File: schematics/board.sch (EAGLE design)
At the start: 25 parts, among them IC1 MEGA8-P, M1 PSMN017-30ELL-V, M2 PSMN017-30ELL-V, M3 PSMN017-30ELL-V

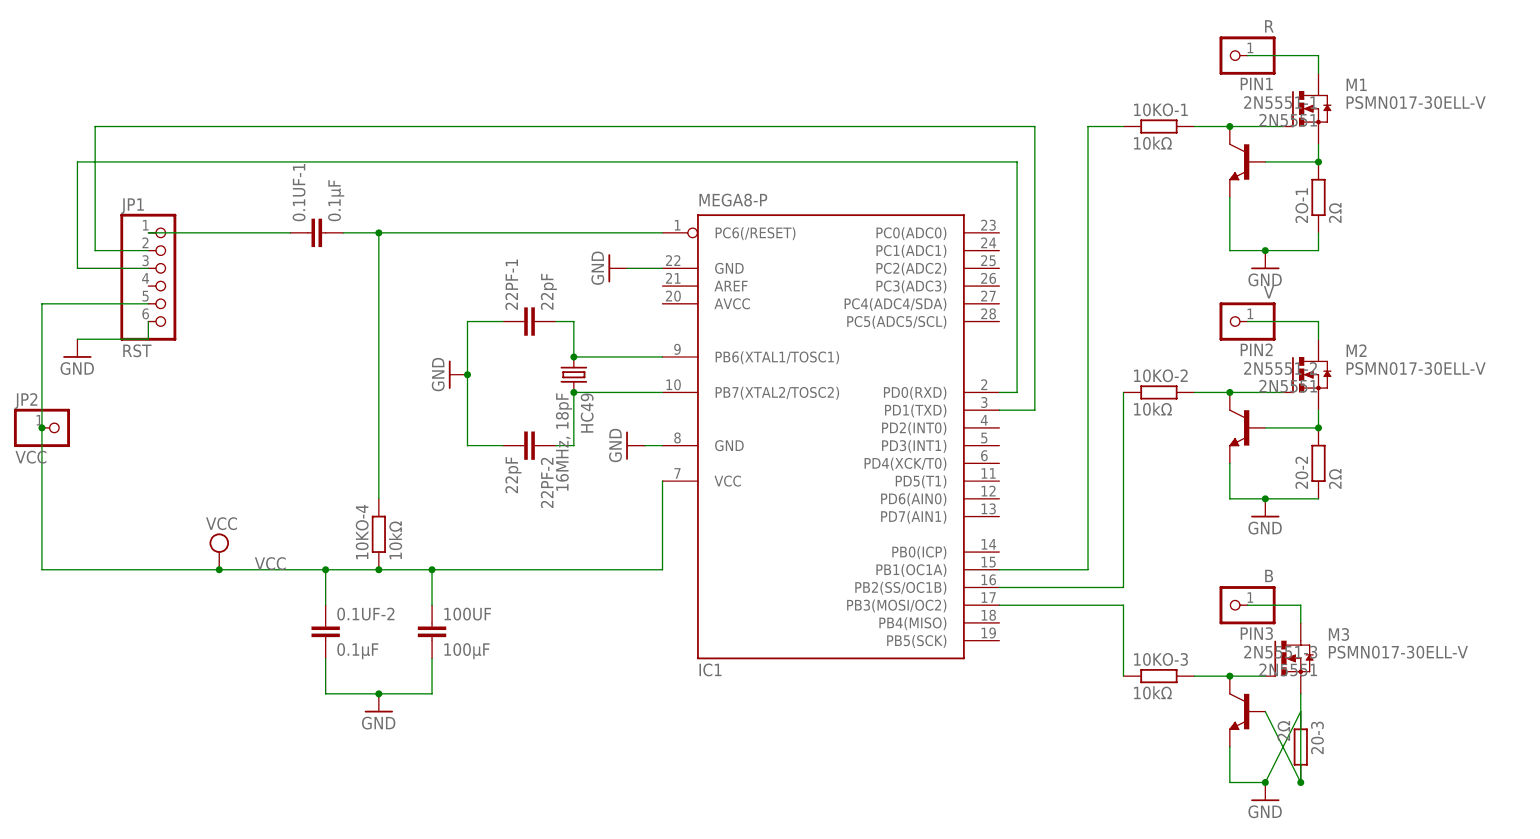
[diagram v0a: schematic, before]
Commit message: Ajoute alim & logo sur la PCB
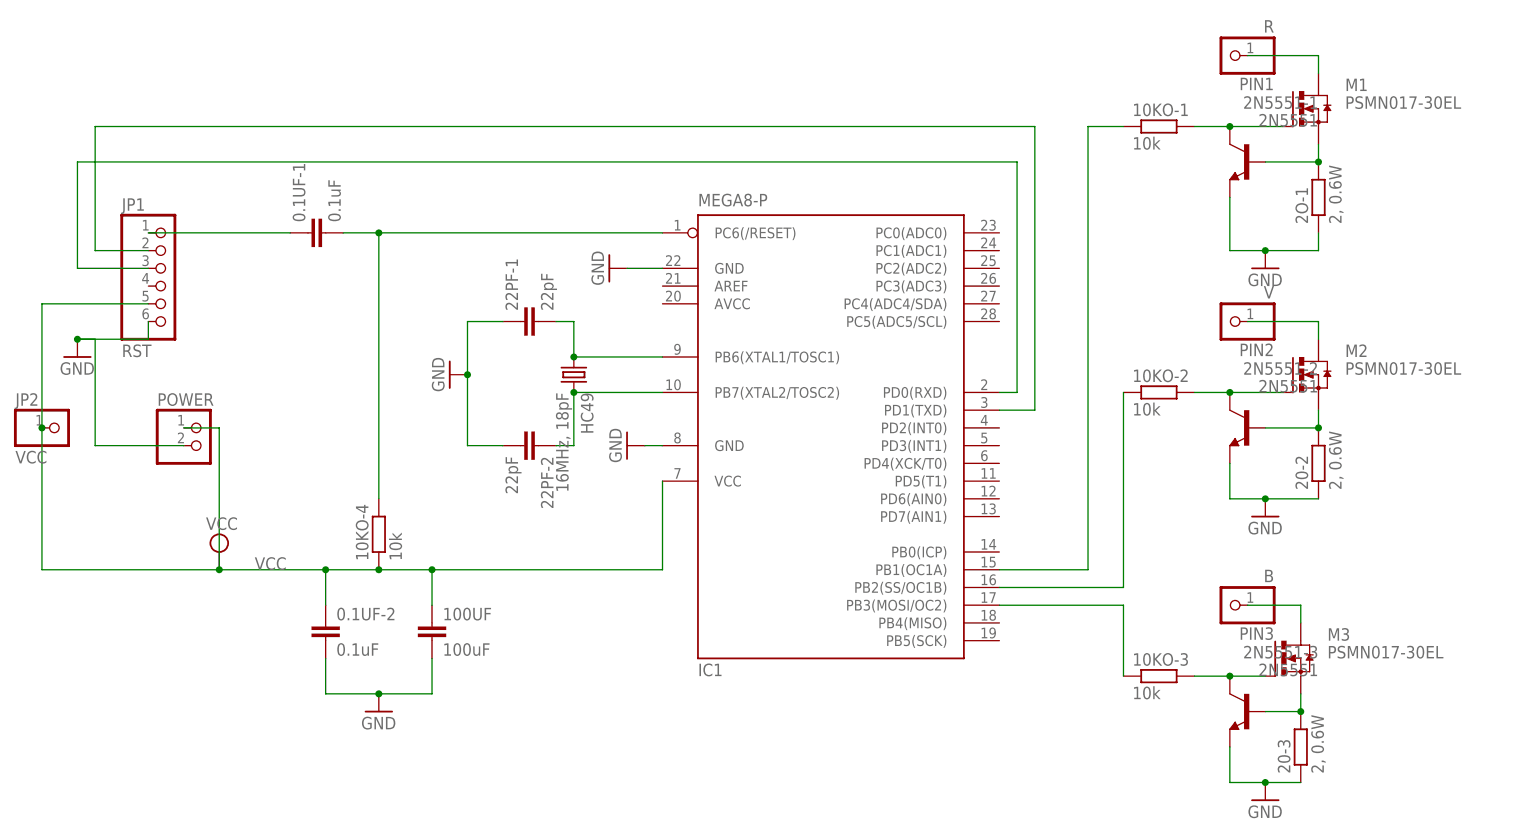
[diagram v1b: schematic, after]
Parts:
- added POWER: (no value), pinhead:PINHD-1X2
- 0.1UF-1, 0.1UF-2: value 0.1μF -> 0.1uF
- 100UF: value 100μF -> 100uF
- 10KO-1, 10KO-2, 10KO-3, 10KO-4: value 10kΩ -> 10k
- 20-2, 20-3, 2O-1: value 2Ω -> 2, 0.6W
- M1, M2, M3: value PSMN017-30ELL-V -> PSMN017-30EL
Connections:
- net GND: now also POWER.2
- net VCC: now also POWER.1
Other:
- moved on the sheet: 20-3
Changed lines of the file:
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@@
 <parts>
 <part name="IC1" library="atmel" deviceset="MEGA8-P" device=""/>
-<part name="10KO-1" library="rcl" deviceset="R-EU_" device="0207/2V" value="10kΩ"/>
-<part name="10KO-2" library="rcl" deviceset="R-EU_" device="0207/2V" value="10kΩ"/>
-<part name="10KO-3" library="rcl" deviceset="R-EU_" device="0207/2V" value="10kΩ"/>
-<part name="10KO-4" library="rcl" deviceset="R-EU_" device="0207/2V" value="10kΩ"/>
-<part name="2O-1" library="rcl" deviceset="R-EU_" device="0309/V" value="2Ω"/>
-<part name="20-2" library="rcl" deviceset="R-EU_" device="0309/V" value="2Ω"/>
-<part name="20-3" library="rcl" deviceset="R-EU_" device="0309/V" value="2Ω"/>
+<part name="10KO-1" library="rcl" deviceset="R-EU_" device="0207/2V" value="10k"/>
+<part name="10KO-2" library="rcl" deviceset="R-EU_" device="0207/2V" value="10k"/>
+<part name="10KO-3" library="rcl" deviceset="R-EU_" device="0207/2V" value="10k"/>
+<part name="10KO-4" library="rcl" deviceset="R-EU_" device="0207/2V" value="10k"/>
+<part name="2O-1" library="rcl" deviceset="R-EU_" device="0309/V" value="2, 0.6W"/>
+<part name="20-2" library="rcl" deviceset="R-EU_" device="0309/V" value="2, 0.6W"/>
+<part name="20-3" library="rcl" deviceset="R-EU_" device="0309/V" value="2, 0.6W"/>
 <part name="2N5551-1" library="transistor" deviceset="*-NPN-" device="TO92-CBE" technology="2N5551" value="2N5551"/>
 <part name="2N5551-2" library="transistor" deviceset="*-NPN-" device="TO92-CBE" technology="2N5551" value="2N5551"/>
 <part name="2N5551-3" library="transistor" deviceset="*-NPN-" device="TO92-CBE" technology="2N5551" value="2N5551"/>
-<part name="0.1UF-1" library="rcl" deviceset="C-EU" device="025-030X050" value="0.1μF"/>
-<part name="0.1UF-2" library="rcl" deviceset="C-EU" device="025-030X050" value="0.1μF"/>
+<part name="0.1UF-1" library="rcl" deviceset="C-EU" device="025-030X050" value="0.1uF"/>
+<part name="0.1UF-2" library="rcl" deviceset="C-EU" device="025-030X050" value="0.1uF"/>
 <part name="22PF-2" library="rcl" deviceset="C-EU" device="025-030X050" value="22pF"/>
 <part name="22PF-1" library="rcl" deviceset="C-EU" device="025-030X050" value="22pF"/>
-<part name="100UF" library="rcl" deviceset="C-EU" device="025-050X050" value="100μF"/>
+<part name="100UF" library="rcl" deviceset="C-EU" device="025-050X050" value="100uF"/>
 <part name="HC49" library="crystal" deviceset="CRYSTAL" device="HC49S" value="16MHz, 18pF"/>
 <part name="GND1" library="supply1" deviceset="GND" device=""/>
@@
 <part name="PIN2" library="pinhead" deviceset="PINHD-1X1" device="" value="V"/>
 <part name="PIN3" library="pinhead" deviceset="PINHD-1X1" device="" value="B"/>
-<part name="M1" library="hackens" deviceset="PSMN017-30EL" device="L-V"/>
-<part name="M2" library="hackens" deviceset="PSMN017-30EL" device="L-V"/>
-<part name="M3" library="hackens" deviceset="PSMN017-30EL" device="L-V"/>
+<part name="M1" library="hackens" deviceset="PSMN017-30EL" device="L-V" value="PSMN017-30EL"/>
+<part name="M2" library="hackens" deviceset="PSMN017-30EL" device="L-V" value="PSMN017-30EL"/>
+<part name="M3" library="hackens" deviceset="PSMN017-30EL" device="L-V" value="PSMN017-30EL"/>
+<part name="POWER" library="pinhead" deviceset="PINHD-1X2" device=""/>
 </parts>
 <sheets>
@@
 <instance part="2O-1" gate="G$1" x="149.86" y="93.98" rot="R90"/>
 <instance part="20-2" gate="G$1" x="149.86" y="55.88" rot="R90"/>
-<instance part="20-3" gate="G$1" x="147.32" y="15.24" rot="R270"/>
+<instance part="20-3" gate="G$1" x="147.32" y="15.24" rot="R90"/>
 <instance part="2N5551-1" gate="G$1" x="139.7" y="99.06" rot="MR0"/>
 <instance part="2N5551-2" gate="G$1" x="139.7" y="60.96" rot="MR0"/>
@@
 <instance part="M2" gate="G$1" x="147.32" y="68.58"/>
 <instance part="M3" gate="G$1" x="144.78" y="27.94"/>
+<instance part="POWER" gate="G$1" x="-10.16" y="58.42"/>
 </instances>
 <busses>
@@
 <wire x1="137.16" y1="10.16" x2="142.24" y2="10.16" width="0.1524" layer="91"/>
 <pinref part="20-3" gate="G$1" pin="1"/>
-<wire x1="142.24" y1="10.16" x2="147.32" y2="20.32" width="0.1524" layer="91"/>
+<wire x1="142.24" y1="10.16" x2="147.32" y2="10.16" width="0.1524" layer="91"/>
 <junction x="142.24" y="10.16"/>
 </segment>
@@
 <wire x1="-27.94" y1="73.66" x2="-17.78" y2="73.66" width="0.1524" layer="91"/>
 <wire x1="-17.78" y1="73.66" x2="-17.78" y2="76.2" width="0.1524" layer="91"/>
+<wire x1="-27.94" y1="73.66" x2="-25.4" y2="73.66" width="0.1524" layer="91"/>
+<wire x1="-25.4" y1="73.66" x2="-25.4" y2="58.42" width="0.1524" layer="91"/>
+<junction x="-27.94" y="73.66"/>
+<pinref part="POWER" gate="G$1" pin="2"/>
+<wire x1="-25.4" y1="58.42" x2="-12.7" y2="58.42" width="0.1524" layer="91"/>
 </segment>
 <segment>
@@
 <pinref part="2N5551-3" gate="G$1" pin="B"/>
 <pinref part="20-3" gate="G$1" pin="2"/>
-<wire x1="142.24" y1="20.32" x2="147.32" y2="10.16" width="0.1524" layer="91"/>
-<wire x1="147.32" y1="10.16" x2="147.32" y2="22.86" width="0.1524" layer="91"/>
-<junction x="147.32" y="10.16"/>
+<wire x1="142.24" y1="20.32" x2="147.32" y2="20.32" width="0.1524" layer="91"/>
+<wire x1="147.32" y1="20.32" x2="147.32" y2="22.86" width="0.1524" layer="91"/>
+<junction x="147.32" y="20.32"/>
 <pinref part="M3" gate="G$1" pin="S"/>
 </segment>
@@
 <junction x="-33.02" y="60.96"/>
 <junction x="-7.62" y="40.64"/>
-</segment>
-</net>
+<wire x1="-7.62" y1="40.64" x2="-7.62" y2="60.96" width="0.1524" layer="91"/>
+<pinref part="POWER" gate="G$1" pin="1"/>
+<wire x1="-7.62" y1="60.96" x2="-12.7" y2="60.96" width="0.1524" layer="91"/>
+</segment>
+</net>

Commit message: Ajout pins upload
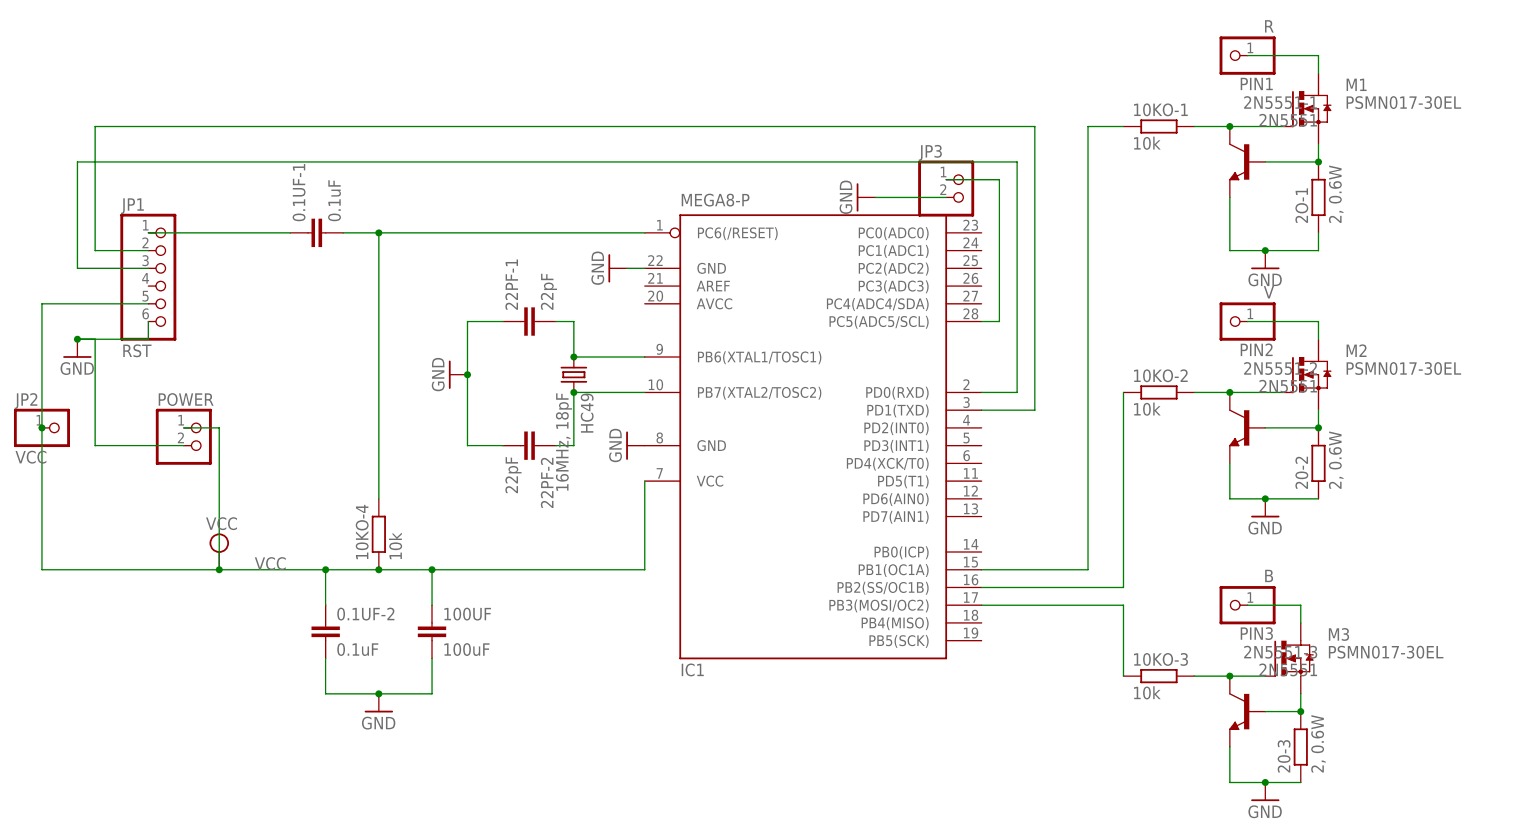
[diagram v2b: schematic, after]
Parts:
- added JP3: (no value), pinhead:PINHD-1X2
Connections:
- new net N$19: IC1.PC5(ADC5/SCL), JP3.1
- net GND: now also JP3.2
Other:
- moved on the sheet: IC1
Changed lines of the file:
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@@
 <part name="M3" library="hackens" deviceset="PSMN017-30EL" device="L-V" value="PSMN017-30EL"/>
 <part name="POWER" library="pinhead" deviceset="PINHD-1X2" device=""/>
+<part name="JP3" library="pinhead" deviceset="PINHD-1X2" device=""/>
+<part name="GND9" library="supply1" deviceset="GND" device=""/>
 </parts>
 <sheets>
@@
 </plain>
 <instances>
-<instance part="IC1" gate="G$1" x="78.74" y="60.96"/>
+<instance part="IC1" gate="G$1" x="76.2" y="60.96"/>
 <instance part="10KO-1" gate="G$1" x="127" y="104.14"/>
 <instance part="10KO-2" gate="G$1" x="127" y="66.04"/>
@@
 <instance part="M3" gate="G$1" x="144.78" y="27.94"/>
 <instance part="POWER" gate="G$1" x="-10.16" y="58.42"/>
+<instance part="JP3" gate="G$1" x="99.06" y="93.98"/>
+<instance part="GND9" gate="1" x="83.82" y="93.98" rot="R270"/>
 </instances>
 <busses>
@@
 <pinref part="GND4" gate="1" pin="GND"/>
 <pinref part="IC1" gate="G$1" pin="GND"/>
-<wire x1="50.8" y1="83.82" x2="55.88" y2="83.82" width="0.1524" layer="91"/>
+<wire x1="50.8" y1="83.82" x2="53.34" y2="83.82" width="0.1524" layer="91"/>
 </segment>
 <segment>
 <pinref part="IC1" gate="G$1" pin="GND@1"/>
 <pinref part="GND5" gate="1" pin="GND"/>
-<wire x1="55.88" y1="58.42" x2="53.34" y2="58.42" width="0.1524" layer="91"/>
 </segment>
 <segment>
@@
 <wire x1="27.94" y1="76.2" x2="33.02" y2="76.2" width="0.1524" layer="91"/>
 </segment>
+<segment>
+<pinref part="JP3" gate="G$1" pin="2"/>
+<wire x1="96.52" y1="93.98" x2="86.36" y2="93.98" width="0.1524" layer="91"/>
+<pinref part="GND9" gate="1" pin="GND"/>
+</segment>
 </net>
 <net name="N$5" class="0">
@@
 <wire x1="10.16" y1="88.9" x2="15.24" y2="88.9" width="0.1524" layer="91"/>
 <pinref part="10KO-4" gate="G$1" pin="2"/>
-<wire x1="15.24" y1="88.9" x2="55.88" y2="88.9" width="0.1524" layer="91"/>
+<wire x1="15.24" y1="88.9" x2="53.34" y2="88.9" width="0.1524" layer="91"/>
 <wire x1="15.24" y1="50.8" x2="15.24" y2="88.9" width="0.1524" layer="91"/>
 <junction x="15.24" y="88.9"/>
@@
 <segment>
 <pinref part="IC1" gate="G$1" pin="PB1(OC1A)"/>
-<wire x1="104.14" y1="40.64" x2="116.84" y2="40.64" width="0.1524" layer="91"/>
+<wire x1="101.6" y1="40.64" x2="116.84" y2="40.64" width="0.1524" layer="91"/>
 <wire x1="116.84" y1="40.64" x2="116.84" y2="104.14" width="0.1524" layer="91"/>
 <pinref part="10KO-1" gate="G$1" pin="1"/>
@@
 <pinref part="IC1" gate="G$1" pin="PB2(SS/OC1B)"/>
 <pinref part="10KO-2" gate="G$1" pin="1"/>
-<wire x1="104.14" y1="38.1" x2="121.92" y2="38.1" width="0.1524" layer="91"/>
+<wire x1="101.6" y1="38.1" x2="121.92" y2="38.1" width="0.1524" layer="91"/>
 <wire x1="121.92" y1="38.1" x2="121.92" y2="66.04" width="0.1524" layer="91"/>
 </segment>
@@
 <pinref part="IC1" gate="G$1" pin="PB3(MOSI/OC2)"/>
 <pinref part="10KO-3" gate="G$1" pin="1"/>
-<wire x1="104.14" y1="35.56" x2="121.92" y2="35.56" width="0.1524" layer="91"/>
+<wire x1="101.6" y1="35.56" x2="121.92" y2="35.56" width="0.1524" layer="91"/>
 <wire x1="121.92" y1="35.56" x2="121.92" y2="25.4" width="0.1524" layer="91"/>
 </segment>
@@
 <wire x1="22.86" y1="40.64" x2="22.86" y2="35.56" width="0.1524" layer="91"/>
 <pinref part="IC1" gate="G$1" pin="VCC@1"/>
-<wire x1="22.86" y1="40.64" x2="55.88" y2="40.64" width="0.1524" layer="91"/>
-<wire x1="55.88" y1="40.64" x2="55.88" y2="53.34" width="0.1524" layer="91"/>
+<wire x1="22.86" y1="40.64" x2="53.34" y2="40.64" width="0.1524" layer="91"/>
+<wire x1="53.34" y1="40.64" x2="53.34" y2="53.34" width="0.1524" layer="91"/>
 <junction x="22.86" y="40.64"/>
 <pinref part="SUPPLY2" gate="G$1" pin="VCC"/>
@@
 <wire x1="109.22" y1="104.14" x2="109.22" y2="63.5" width="0.1524" layer="91"/>
 <pinref part="IC1" gate="G$1" pin="PD1(TXD)"/>
-<wire x1="109.22" y1="63.5" x2="104.14" y2="63.5" width="0.1524" layer="91"/>
+<wire x1="109.22" y1="63.5" x2="101.6" y2="63.5" width="0.1524" layer="91"/>
 </segment>
 </net>
@@
 <segment>
 <pinref part="IC1" gate="G$1" pin="PD0(RXD)"/>
-<wire x1="104.14" y1="66.04" x2="106.68" y2="66.04" width="0.1524" layer="91"/>
+<wire x1="101.6" y1="66.04" x2="106.68" y2="66.04" width="0.1524" layer="91"/>
 <wire x1="106.68" y1="66.04" x2="106.68" y2="99.06" width="0.1524" layer="91"/>
 <wire x1="106.68" y1="99.06" x2="-27.94" y2="99.06" width="0.1524" layer="91"/>
@@
 <pinref part="IC1" gate="G$1" pin="PB6(XTAL1/TOSC1)"/>
 <pinref part="HC49" gate="G$1" pin="1"/>
-<wire x1="55.88" y1="71.12" x2="43.18" y2="71.12" width="0.1524" layer="91"/>
+<wire x1="53.34" y1="71.12" x2="43.18" y2="71.12" width="0.1524" layer="91"/>
 <wire x1="43.18" y1="71.12" x2="43.18" y2="76.2" width="0.1524" layer="91"/>
 <junction x="43.18" y="71.12"/>
@@
 <pinref part="IC1" gate="G$1" pin="PB7(XTAL2/TOSC2)"/>
 <pinref part="HC49" gate="G$1" pin="2"/>
-<wire x1="55.88" y1="66.04" x2="43.18" y2="66.04" width="0.1524" layer="91"/>
+<wire x1="53.34" y1="66.04" x2="43.18" y2="66.04" width="0.1524" layer="91"/>
 <wire x1="43.18" y1="66.04" x2="43.18" y2="58.42" width="0.1524" layer="91"/>
 <junction x="43.18" y="66.04"/>
@@
 </segment>
 </net>
+<net name="N$19" class="0">
+<segment>
+<pinref part="IC1" gate="G$1" pin="PC5(ADC5/SCL)"/>
+<wire x1="101.6" y1="76.2" x2="104.14" y2="76.2" width="0.1524" layer="91"/>
+<wire x1="104.14" y1="76.2" x2="104.14" y2="96.52" width="0.1524" layer="91"/>
+<pinref part="JP3" gate="G$1" pin="1"/>
+<wire x1="104.14" y1="96.52" x2="96.52" y2="96.52" width="0.1524" layer="91"/>
+</segment>
+</net>

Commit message: Connecte AVCC et VCC
D'après la datasheet atmel
(http://www.farnell.com/datasheets/1698185.pdf )
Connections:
- net VCC: now also IC1.AVCC
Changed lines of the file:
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@@
 <pinref part="POWER" gate="G$1" pin="1"/>
 <wire x1="-7.62" y1="60.96" x2="-12.7" y2="60.96" width="0.1524" layer="91"/>
+<pinref part="IC1" gate="G$1" pin="AVCC"/>
+<wire x1="53.34" y1="78.74" x2="22.86" y2="78.74" width="0.1524" layer="91"/>
+<wire x1="22.86" y1="78.74" x2="22.86" y2="40.64" width="0.1524" layer="91"/>
 </segment>
 </net>
